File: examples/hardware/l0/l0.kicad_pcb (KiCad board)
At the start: 2 copper layers, 20.3 x 24.5 mm, 46 parts, among them J1 DF11-8DP-2DS(24), J2 DF11-8DP-2DS(24), J3 µUSB_B, J4 Header6Contacts, J5 Header6Contacts, Q1 BC846BWT1G, U1 ST3485ECDR, U2 STM32F072CBU, U3 TPS5401

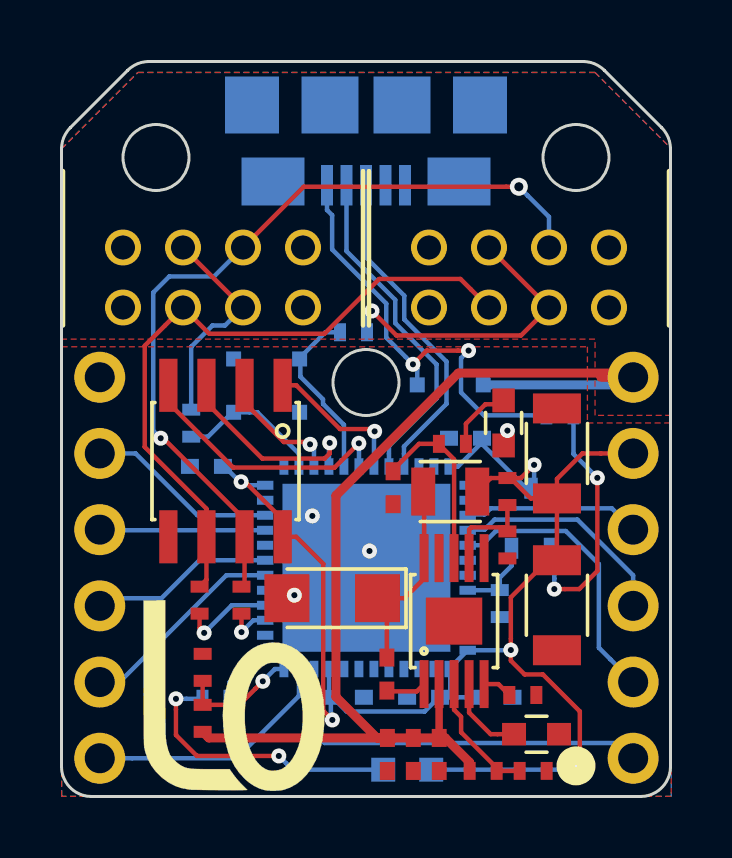
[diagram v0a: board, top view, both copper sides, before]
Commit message: Update some hardware project to the new Kicad version
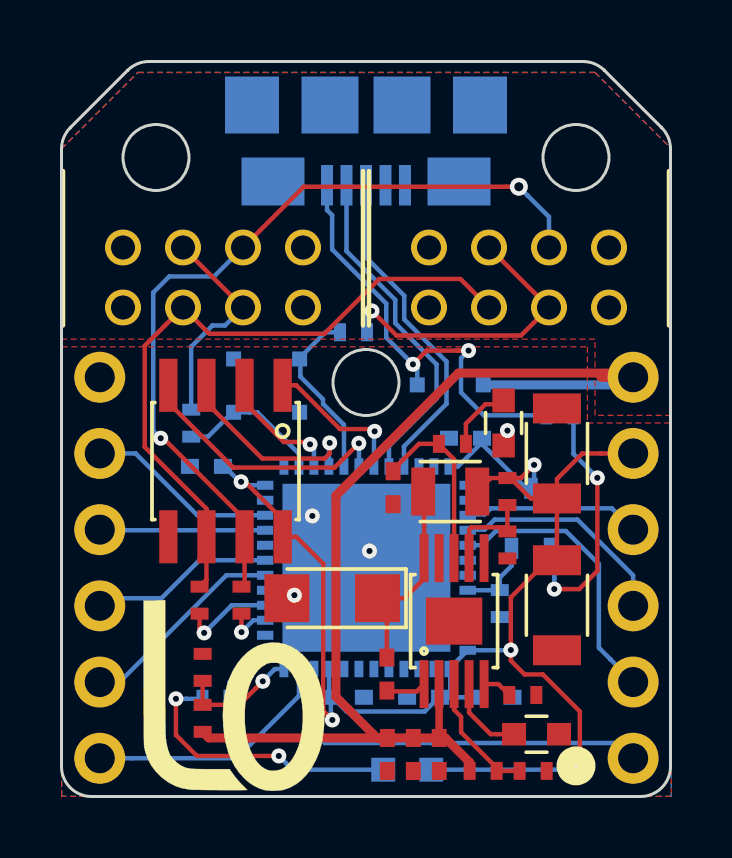
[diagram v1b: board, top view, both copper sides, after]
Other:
- outline, holes or cut-outs redrawn
- net class Default removed
- net class Vin removed
